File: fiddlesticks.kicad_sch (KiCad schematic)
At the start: 63 parts, among them J1 Conn_01x02_Pin, J2 Conn_01x04_Pin, J4 TYPE-C-31-M-12, J5 Conn_02x04_Counter_Clockwise, J6 Conn_01x05_Pin, SW1 SW_Push, SW2 SW_Push, U1 MCP1640Bx-xCHY, U2 STM32F411CEUx, U3 SPX3819M5-L-3-3, U4 USBLC6-2SC6, Y1 8MHz 12pF

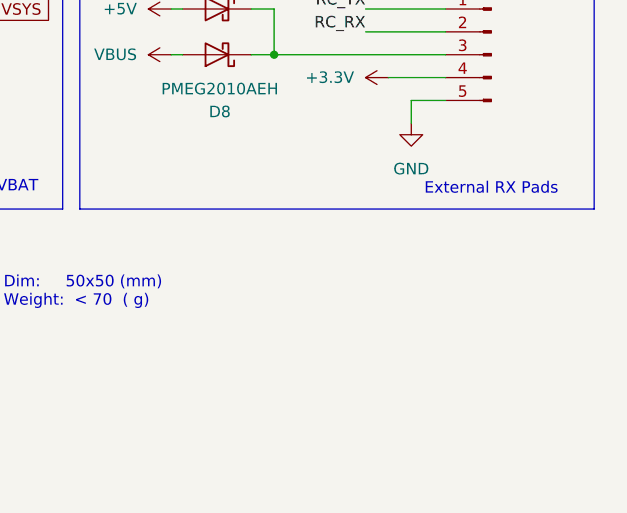
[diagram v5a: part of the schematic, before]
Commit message: added vias under MCU, added silk screen for SWD
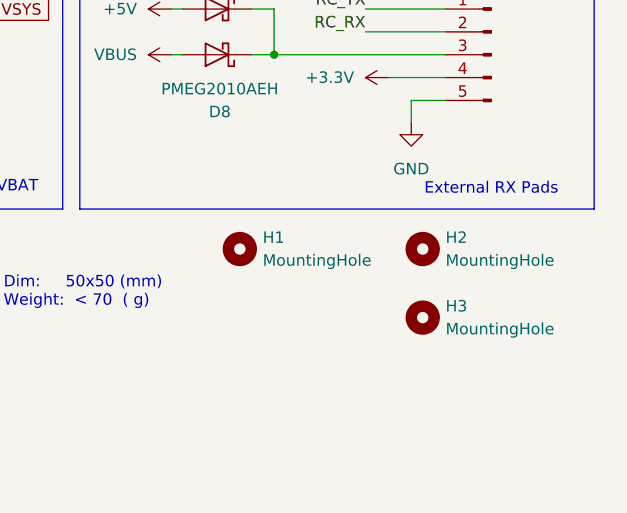
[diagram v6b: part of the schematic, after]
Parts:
- added H1, H2, H3: MountingHole, MountingHole:MountingHole_2.2mm_M2, symbol Mechanical:MountingHole
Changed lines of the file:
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@@
 	)
 	(symbol
+		(lib_id "Mechanical:MountingHole")
+		(at 264.16 176.53 0)
+		(unit 1)
+		(exclude_from_sim no)
+		(in_bom no)
+		(on_board yes)
+		(dnp no)
+		(fields_autoplaced yes)
+		(property "Reference" "H3"
+			(at 266.7 175.2599 0)
+			(effects
+				(font
+					(size 1.27 1.27)
+				)
+				(justify left)
+			)
+		)
+		(property "Value" "MountingHole"
+			(at 266.7 177.7999 0)
+			(effects
+				(font
+					(size 1.27 1.27)
+				)
+				(justify left)
+			)
+		)
+		(property "Footprint" "MountingHole:MountingHole_2.2mm_M2"
+			(at 264.16 176.53 0)
+			(effects
+				(font
+					(size 1.27 1.27)
+				)
+				(hide yes)
+			)
+		)
+		(property "Datasheet" "~"
+			(at 264.16 176.53 0)
+			(effects
+				(font
+					(size 1.27 1.27)
+				)
+				(hide yes)
+			)
+		)
+		(property "Description" "Mounting Hole without connection"
+			(at 264.16 176.53 0)
+			(effects
+				(font
+					(size 1.27 1.27)
+				)
+				(hide yes)
+			)
+		)
+		(instances
+			(project "fiddlesticks"
+				(path "/556ec640-bea9-4fdd-87e6-542e7daf24cf"
+					(reference "H3")
+					(unit 1)
+				)
+			)
+		)
+	)
+	(symbol
+		(lib_id "Mechanical:MountingHole")
+		(at 264.16 168.91 0)
+		(unit 1)
+		(exclude_from_sim no)
+		(in_bom no)
+		(on_board yes)
+		(dnp no)
+		(fields_autoplaced yes)
+		(property "Reference" "H2"
+			(at 266.7 167.6399 0)
+			(effects
+				(font
+					(size 1.27 1.27)
+				)
+				(justify left)
+			)
+		)
+		(property "Value" "MountingHole"
+			(at 266.7 170.1799 0)
+			(effects
+				(font
+					(size 1.27 1.27)
+				)
+				(justify left)
+			)
+		)
+		(property "Footprint" "MountingHole:MountingHole_2.2mm_M2"
+			(at 264.16 168.91 0)
+			(effects
+				(font
+					(size 1.27 1.27)
+				)
+				(hide yes)
+			)
+		)
+		(property "Datasheet" "~"
+			(at 264.16 168.91 0)
+			(effects
+				(font
+					(size 1.27 1.27)
+				)
+				(hide yes)
+			)
+		)
+		(property "Description" "Mounting Hole without connection"
+			(at 264.16 168.91 0)
+			(effects
+				(font
+					(size 1.27 1.27)
+				)
+				(hide yes)
+			)
+		)
+		(instances
+			(project "fiddlesticks"
+				(path "/556ec640-bea9-4fdd-87e6-542e7daf24cf"
+					(reference "H2")
+					(unit 1)
+				)
+			)
+		)
+	)
+	(symbol
 		(lib_id "power:GND")
 		(at 102.87 31.75 0)
@@
 					(unit 1)
 				)
+			)
+		)
+	)
+	(symbol
+		(lib_id "Mechanical:MountingHole")
+		(at 243.84 168.91 0)
+		(unit 1)
+		(exclude_from_sim no)
+		(in_bom no)
+		(on_board yes)
+		(dnp no)
+		(fields_autoplaced yes)
+		(property "Reference" "H1"
+			(at 246.38 167.6399 0)
+			(effects
+				(font
+					(size 1.27 1.27)
+				)
+				(justify left)
+			)
+		)
+		(property "Value" "MountingHole"
+			(at 246.38 170.1799 0)
+			(effects
+				(font
+					(size 1.27 1.27)
+				)
+				(justify left)
+			)
+		)
+		(property "Footprint" "MountingHole:MountingHole_2.2mm_M2"
+			(at 243.84 168.91 0)
+			(effects
+				(font
+					(size 1.27 1.27)
+				)
+				(hide yes)
+			)
+		)
+		(property "Datasheet" "~"
+			(at 243.84 168.91 0)
+			(effects
+				(font
+					(size 1.27 1.27)
+				)
+				(hide yes)
+			)
+		)
+		(property "Description" "Mounting Hole without connection"
+			(at 243.84 168.91 0)
+			(effects
+				(font
+					(size 1.27 1.27)
+				)
+				(hide yes)
+			)
+		)
+		(instances
+			(project ""
+				(path "/556ec640-bea9-4fdd-87e6-542e7daf24cf"
+					(reference "H1")
+					(unit 1)
+				)

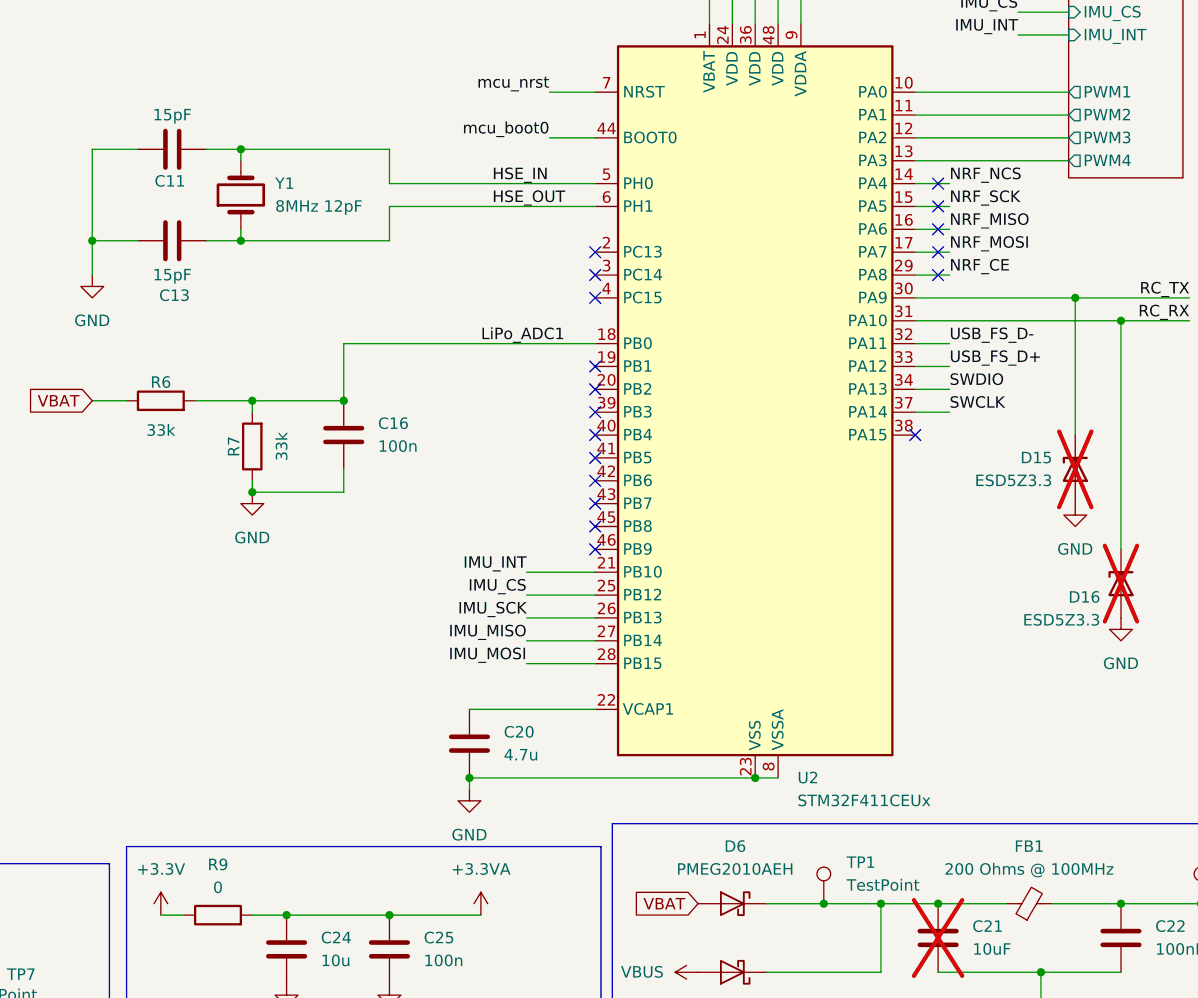
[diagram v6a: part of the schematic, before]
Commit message: fixed some more routing
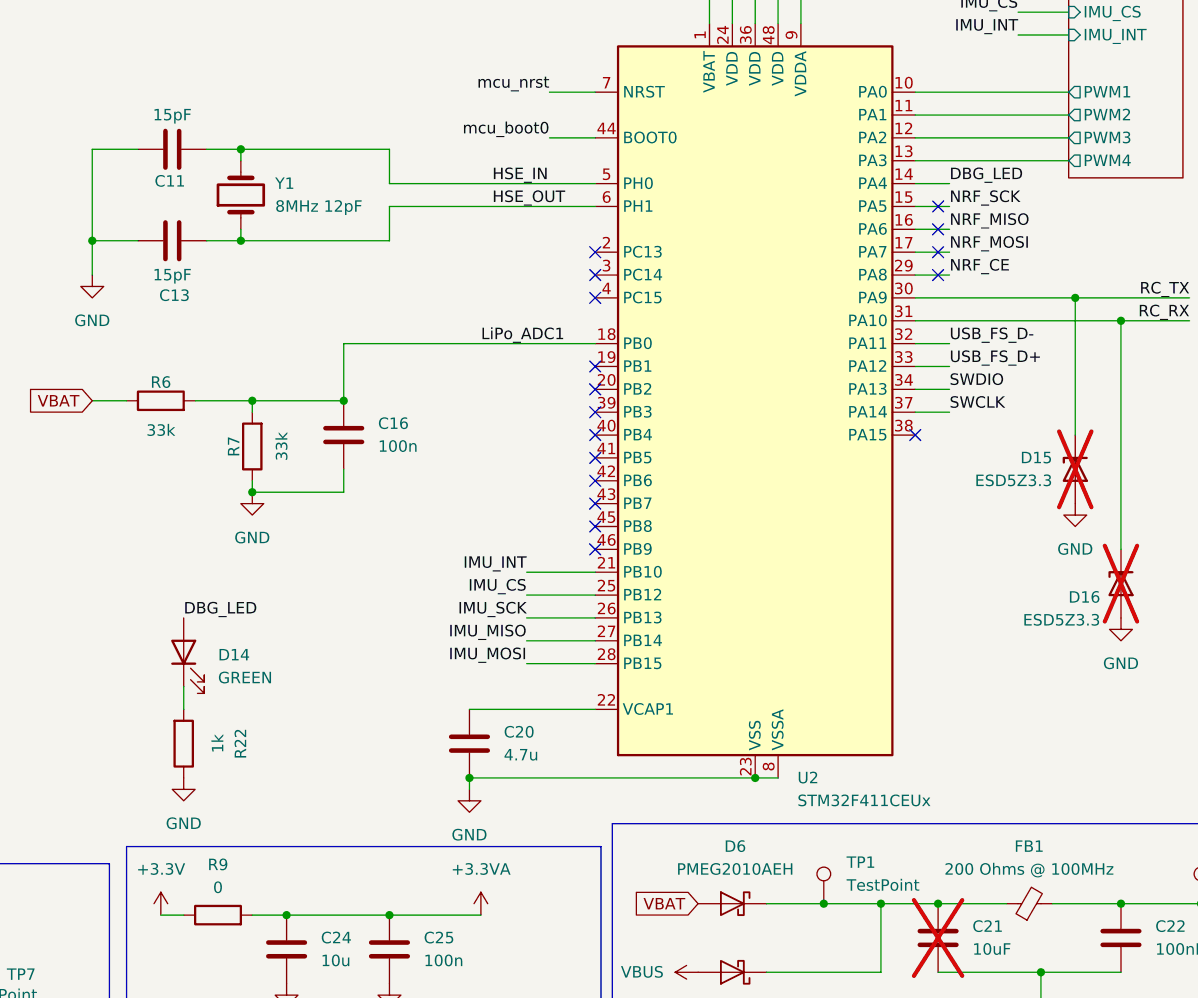
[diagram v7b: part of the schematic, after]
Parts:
- added D14: GREEN, LED_SMD:LED_0603_1608Metric_Pad1.05x0.95mm_HandSolder, symbol Device:LED
- added R22: 1k, Resistor_SMD:R_0603_1608Metric_Pad0.98x0.95mm_HandSolder, symbol Device:R
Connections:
- net GND: now also R22.1
- net NRF_NCS: no longer U2.14 (PA4)
- new net: D14.1 (K), R22.2
- new net DBG_LED: D14.2 (A), U2.14 (PA4)
- no-connect marks 21 -> 20
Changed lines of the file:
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@@
 	)
 	(no_connect
-		(at 172.72 62.23)
-	)
-	(no_connect
 		(at 134.62 69.85)
 	)
@@
 	(wire
 		(pts
+			(xy 88.9 118.11) (xy 88.9 120.65)
+		)
+		(stroke
+			(width 0)
+			(type default)
+		)
+	)
+	(wire
+		(pts
 			(xy 256.54 105.41) (xy 270.51 105.41)
 		)
@@
 		)
 	)
+	(label "DBG_LED"
+		(at 88.9 110.49 0)
+		(effects
+			(font
+				(size 1.27 1.27)
+			)
+			(justify left bottom)
+		)
+	)
 	(label "SWDIO"
 		(at 36.83 97.79 0)
@@
 		)
 	)
+	(label "DBG_LED"
+		(at 173.99 62.23 0)
+		(effects
+			(font
+				(size 1.27 1.27)
+			)
+			(justify left bottom)
+		)
+	)
 	(label "RC_RX"
 		(at 200.66 77.47 180)
@@
 		)
 	)
-	(label "NRF_NCS"
-		(at 173.99 62.23 0)
-		(effects
-			(font
-				(size 1.27 1.27)
-			)
-			(justify left bottom)
-		)
-	)
 	(label "IMU_MOSI"
 		(at 181.61 40.64 180)
@@
 	(symbol
 		(lib_id "power:GND")
+		(at 88.9 128.27 0)
+		(mirror y)
+		(unit 1)
+		(exclude_from_sim no)
+		(in_bom yes)
+		(on_board yes)
+		(dnp no)
+		(fields_autoplaced yes)
+		(property "Reference" "#PWR061"
+			(at 88.9 134.62 0)
+			(effects
+				(font
+					(size 1.27 1.27)
+				)
+				(hide yes)
+			)
+		)
+		(property "Value" "GND"
+			(at 88.9 133.35 0)
+			(effects
+				(font
+					(size 1.27 1.27)
+				)
+			)
+		)
+		(property "Footprint" ""
+			(at 88.9 128.27 0)
+			(effects
+				(font
+					(size 1.27 1.27)
+				)
+				(hide yes)
+			)
+		)
+		(property "Datasheet" ""
+			(at 88.9 128.27 0)
+			(effects
+				(font
+					(size 1.27 1.27)
+				)
+				(hide yes)
+			)
+		)
+		(property "Description" "Power symbol creates a global label with name \"GND\" , ground"
+			(at 88.9 128.27 0)
+			(effects
+				(font
+					(size 1.27 1.27)
+				)
+				(hide yes)
+			)
+		)
+		(pin "1"
+		)
+		(instances
+			(project "fiddlesticks"
+				(path "/556ec640-bea9-4fdd-87e6-542e7daf24cf"
+					(reference "#PWR061")
+					(unit 1)
+				)
+			)
+		)
+	)
+	(symbol
+		(lib_id "power:GND")
 		(at 96.52 96.52 0)
 		(mirror y)
@@
 	)
 	(symbol
+		(lib_id "Device:LED")
+		(at 88.9 114.3 90)
+		(unit 1)
+		(exclude_from_sim no)
+		(in_bom yes)
+		(on_board yes)
+		(dnp no)
+		(fields_autoplaced yes)
+		(property "Reference" "D14"
+			(at 92.71 114.6174 90)
+			(effects
+				(font
+					(size 1.27 1.27)
+				)
+				(justify right)
+			)
+		)
+		(property "Value" "GREEN"
+			(at 92.71 117.1574 90)
+			(effects
+				(font
+					(size 1.27 1.27)
+				)
+				(justify right)
+			)
+		)
+		(property "Footprint" "LED_SMD:LED_0603_1608Metric_Pad1.05x0.95mm_HandSolder"
+			(at 88.9 114.3 0)
+			(effects
+				(font
+					(size 1.27 1.27)
+				)
+				(hide yes)
+			)
+		)
+		(property "Datasheet" "~"
+			(at 88.9 114.3 0)
+			(effects
+				(font
+					(size 1.27 1.27)
+				)
+				(hide yes)
+			)
+		)
+		(property "Description" "Light emitting diode"
+			(at 88.9 114.3 0)
+			(effects
+				(font
+					(size 1.27 1.27)
+				)
+				(hide yes)
+			)
+		)
+		(property "Sim.Pins" "1=K 2=A"
+			(at 88.9 114.3 0)
+			(effects
+				(font
+					(size 1.27 1.27)
+				)
+				(hide yes)
+			)
+		)
+		(pin "1"
+		)
+		(pin "2"
+		)
+		(instances
+			(project "fiddlesticks"
+				(path "/556ec640-bea9-4fdd-87e6-542e7daf24cf"
+					(reference "D14")
+					(unit 1)
+				)
+			)
+		)
+	)
+	(symbol
 		(lib_id "Device:C")
 		(at 274.32 72.39 0)
@@
 					(unit 1)
 				)
+			)
+		)
+	)
+	(symbol
+		(lib_id "Device:R")
+		(at 88.9 124.46 0)
+		(mirror x)
+		(unit 1)
+		(exclude_from_sim no)
+		(in_bom yes)
+		(on_board yes)
+		(dnp no)
+		(property "Reference" "R22"
+			(at 95.25 124.46 90)
+			(effects
+				(font
+					(size 1.27 1.27)
+				)
+			)
+		)
+		(property "Value" "1k"
+			(at 92.71 124.46 90)
+			(effects
+				(font
+					(size 1.27 1.27)
+				)
+			)
+		)
+		(property "Footprint" "Resistor_SMD:R_0603_1608Metric_Pad0.98x0.95mm_HandSolder"
+			(at 87.122 124.46 90)
+			(effects
+				(font
+					(size 1.27 1.27)
+				)
+				(hide yes)
+			)
+		)
+		(property "Datasheet" "~"
+			(at 88.9 124.46 0)
+			(effects
+				(font
+					(size 1.27 1.27)
+				)
+				(hide yes)
+			)
+		)
+		(property "Description" "Resistor"
+			(at 88.9 124.46 0)
+			(effects
+				(font
+					(size 1.27 1.27)
+				)
+				(hide yes)
+			)
+		)
+		(pin "1"
+		)
+		(pin "2"
+		)
+		(instances
+			(project "fiddlesticks"
+				(path "/556ec640-bea9-4fdd-87e6-542e7daf24cf"
+					(reference "R22")
+					(unit 1)
+				)
